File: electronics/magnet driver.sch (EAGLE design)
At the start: 16 parts, among them K1 G2RL-2DC12, Q1 RK7002BMT116, Q2 DMN1019UVT-7DMN1019UVT-7, Q3 PMBT2222A,215PMBT2222A,215

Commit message: Added MCU
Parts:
- added C6: 0.1uF, Zach:CAPACITOR0805
- added C7, C8: 10pF, Zach:CAPACITOR0805
- added J1: 1-770968-0, Zach:1-770968-0
- added J2: DF1BZ-8DP-2.5DSA, Zach:DF1BZ-8DP-2.5DSA
- added U1: ATMEGA328PB32-TQFP, Zach:ATMEGA328PB32-TQFP
- added XTAL1: 8 MHz, Zach:XRCGB
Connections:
- new net !RESET: J2.!RESET, U1.PC6
- new net MISO: J2.MISO, U1.PB4
- new net MOSI: J2.MOSI, U1.PB3
- new net RX: J2.RX, U1.PD0
- new net SCL: J1.SCL, U1.PC5
- new net SCLK: J2.SCLK, U1.PB5
- new net SDA: J1.SDA, U1.PC4
- new net TX: J2.TX, U1.PD1
- new net XTAL1: C7.P$2, U1.PB6, XTAL1.P$1
- new net XTAL2: C8.P$2, U1.PB7, XTAL1.P$2
- net +3V3: now also C6.P$2, J1.+3V3, J2.+3V3, U1.AREF, U1.AVCC, U1.VCC
- net GND: now also C6.P$1, C7.P$1, C8.P$1, J1.GND, J2.GND, U1.GND

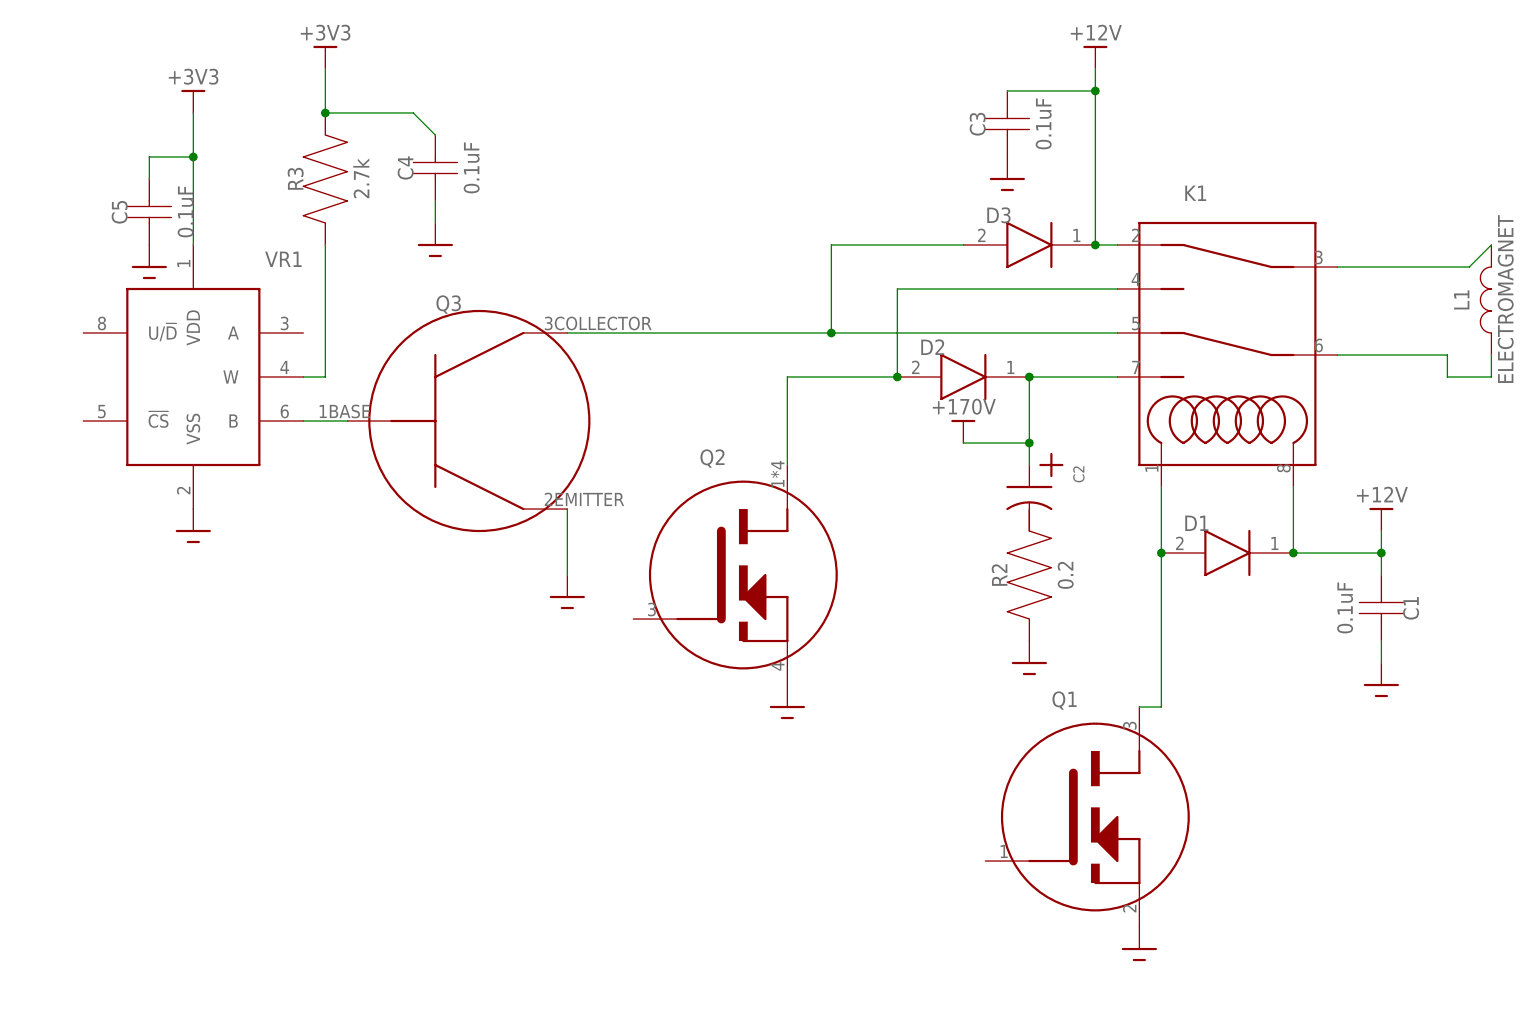
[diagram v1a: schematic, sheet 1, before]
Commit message: Finished magnet driver schematic
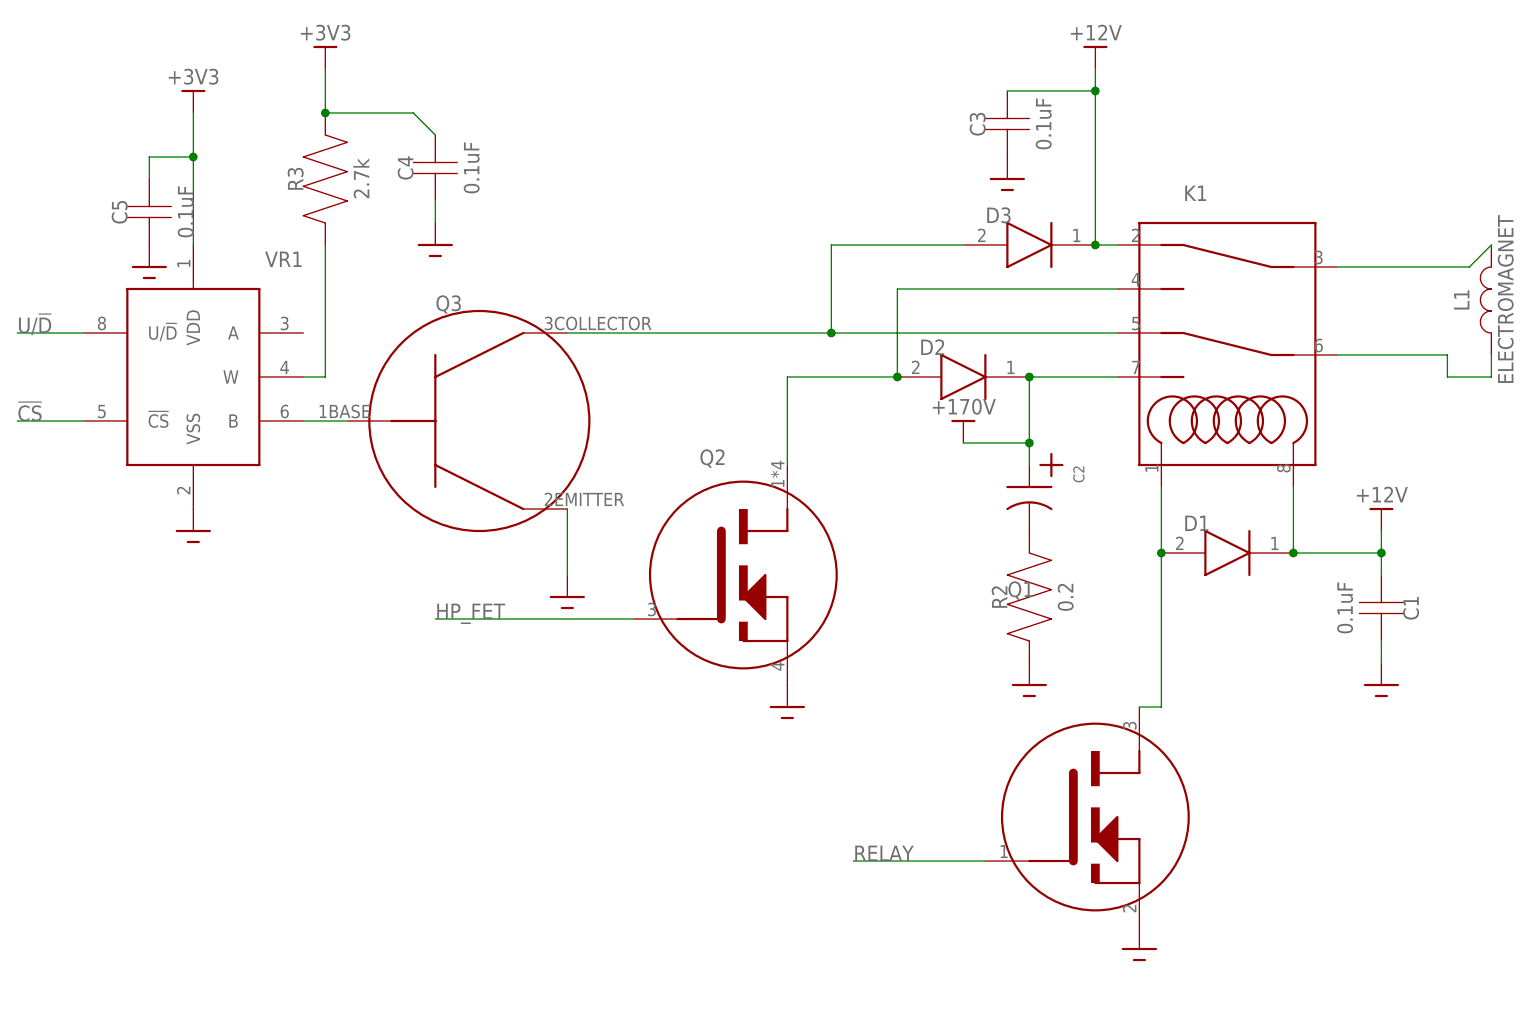
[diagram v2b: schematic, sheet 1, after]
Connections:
- new net !CS: U1.PD4, VR1.!CS
- new net HP_FET: Q2.GATE(1), U1.PD5
- new net N$2: C2.-, R2.P$2
- new net RELAY: Q1.GATE(1), U1.PD6
- new net U/!D: U1.PD3, VR1.U/!D
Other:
- moved on the sheet: R2
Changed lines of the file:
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@@
 <instance part="GND1" gate="1" x="119.38" y="-2.54" smashed="yes"/>
 <instance part="Q1" gate="G$1" x="99.06" y="-12.7" smashed="yes">
-<attribute name="NAME" x="81.28" y="-5.08" size="1.778" layer="95"/>
+<attribute name="NAME" x="76.2" y="7.62" size="1.778" layer="95"/>
 </instance>
 <instance part="GND2" gate="1" x="91.44" y="-33.02" smashed="yes"/>
@@
 <attribute name="NAME" x="66.04" y="35.56" size="1.778" layer="95"/>
 </instance>
-<instance part="GND3" gate="1" x="78.74" y="0" smashed="yes"/>
+<instance part="GND3" gate="1" x="78.74" y="-2.54" smashed="yes"/>
 <instance part="C2" gate="G$1" x="78.74" y="20.32" smashed="yes" rot="R270">
 <attribute name="NAME" x="83.82" y="22.86" size="1.27" layer="95" rot="R270"/>
 <attribute name="VALUE" x="73.66" y="22.86" size="1.27" layer="96" rot="R270"/>
 </instance>
-<instance part="R2" gate="G$1" x="78.74" y="2.54" smashed="yes" rot="R90">
-<attribute name="NAME" x="76.2" y="10.16" size="1.778" layer="95" rot="R90" align="bottom-center"/>
-<attribute name="VALUE" x="83.82" y="10.16" size="1.778" layer="96" rot="R90" align="bottom-center"/>
+<instance part="R2" gate="G$1" x="78.74" y="0" smashed="yes" rot="R90">
+<attribute name="NAME" x="76.2" y="7.62" size="1.778" layer="95" rot="R90" align="bottom-center"/>
+<attribute name="VALUE" x="83.82" y="7.62" size="1.778" layer="96" rot="R90" align="bottom-center"/>
 </instance>
 <instance part="P+2" gate="G$1" x="71.12" y="27.94" smashed="yes">
@@
 <junction x="-17.78" y="58.42"/>
 <pinref part="P+5" gate="G$1" pin="+3V3"/>
+</segment>
+</net>
+<net name="U/!D" class="0">
+<segment>
+<pinref part="VR1" gate="G$1" pin="U/!D"/>
+<wire x1="-30.48" y1="38.1" x2="-38.1" y2="38.1" width="0.1524" layer="91"/>
+<label x="-38.1" y="38.1" size="1.778" layer="95"/>
+</segment>
+</net>
+<net name="!CS" class="0">
+<segment>
+<pinref part="VR1" gate="G$1" pin="!CS"/>
+<wire x1="-30.48" y1="27.94" x2="-38.1" y2="27.94" width="0.1524" layer="91"/>
+<label x="-38.1" y="27.94" size="1.778" layer="95"/>
+</segment>
+</net>
+<net name="HP_FET" class="0">
+<segment>
+<pinref part="Q2" gate="G$1" pin="GATE(1)"/>
+<wire x1="33.02" y1="5.08" x2="10.16" y2="5.08" width="0.1524" layer="91"/>
+<label x="10.16" y="5.08" size="1.778" layer="95"/>
+</segment>
+</net>
+<net name="RELAY" class="0">
+<segment>
+<pinref part="Q1" gate="G$1" pin="GATE(1)"/>
+<wire x1="73.66" y1="-22.86" x2="58.42" y2="-22.86" width="0.1524" layer="91"/>
+<label x="58.42" y="-22.86" size="1.778" layer="95"/>
+</segment>
+</net>
+<net name="N$2" class="0">
+<segment>
+<pinref part="C2" gate="G$1" pin="-"/>
+<pinref part="R2" gate="G$1" pin="P$2"/>
 </segment>
 </net>
@@
 </segment>
 </net>
+<net name="U/!D" class="0">
+<segment>
+<pinref part="U1" gate="G$1" pin="PD3"/>
+<wire x1="68.58" y1="66.04" x2="81.28" y2="66.04" width="0.1524" layer="91"/>
+<label x="71.12" y="66.04" size="1.778" layer="95"/>
+</segment>
+</net>
+<net name="!CS" class="0">
+<segment>
+<pinref part="U1" gate="G$1" pin="PD4"/>
+<wire x1="68.58" y1="63.5" x2="81.28" y2="63.5" width="0.1524" layer="91"/>
+<label x="71.12" y="63.5" size="1.778" layer="95"/>
+</segment>
+</net>
+<net name="HP_FET" class="0">
+<segment>
+<pinref part="U1" gate="G$1" pin="PD5"/>
+<wire x1="68.58" y1="60.96" x2="81.28" y2="60.96" width="0.1524" layer="91"/>
+<label x="71.12" y="60.96" size="1.778" layer="95"/>
+</segment>
+</net>
+<net name="RELAY" class="0">
+<segment>
+<pinref part="U1" gate="G$1" pin="PD6"/>
+<wire x1="68.58" y1="58.42" x2="81.28" y2="58.42" width="0.1524" layer="91"/>
+<label x="71.12" y="58.42" size="1.778" layer="95"/>
+</segment>
+</net>

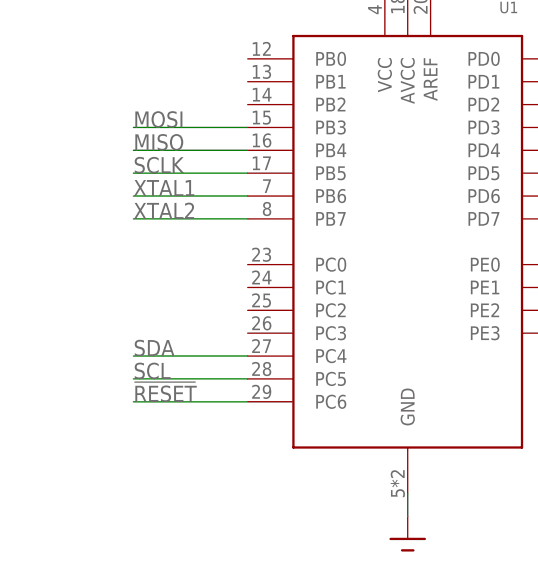
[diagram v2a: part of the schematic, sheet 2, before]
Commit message: Added pull-up on RESET
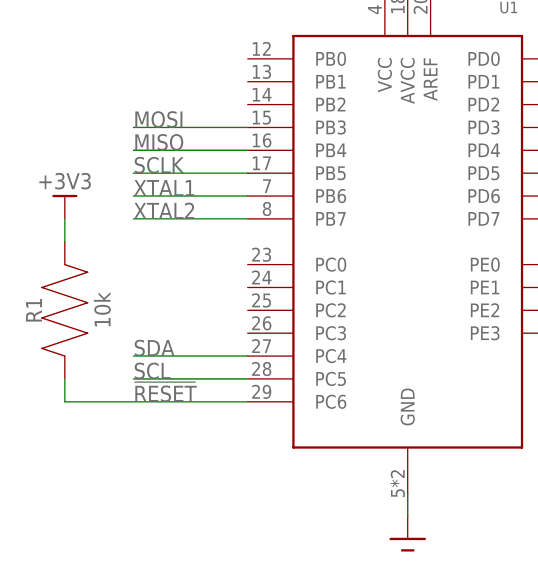
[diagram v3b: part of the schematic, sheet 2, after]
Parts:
- added R1: 10k, Zach:RESISTOR0805
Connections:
- net !RESET: now also R1.P$1
- net +3V3: now also R1.P$2
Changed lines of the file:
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@@
 <part name="GND14" library="Zach" deviceset="GND" device=""/>
 <part name="GND15" library="Zach" deviceset="GND" device=""/>
+<part name="R1" library="Zach" deviceset="RESISTOR" device="0805" value="10k"/>
+<part name="P+10" library="Zach" deviceset="+3V3" device=""/>
 </parts>
 <sheets>
@@
 <instance part="GND14" gate="1" x="86.36" y="22.86" smashed="yes"/>
 <instance part="GND15" gate="1" x="104.14" y="22.86" smashed="yes"/>
+<instance part="R1" gate="G$1" x="12.7" y="38.1" smashed="yes" rot="R90">
+<attribute name="NAME" x="10.16" y="45.72" size="1.778" layer="95" rot="R90" align="bottom-center"/>
+<attribute name="VALUE" x="17.78" y="45.72" size="1.778" layer="96" rot="R90" align="bottom-center"/>
+</instance>
+<instance part="P+10" gate="G$1" x="12.7" y="58.42" smashed="yes">
+<attribute name="VALUE" x="12.7" y="60.96" size="1.778" layer="96" rot="R180" align="bottom-center"/>
+</instance>
 </instances>
 <busses>
@@
 <wire x1="119.38" y1="55.88" x2="121.92" y2="55.88" width="0.1524" layer="91"/>
 </segment>
+<segment>
+<pinref part="R1" gate="G$1" pin="P$2"/>
+<pinref part="P+10" gate="G$1" pin="+3V3"/>
+<wire x1="12.7" y1="55.88" x2="12.7" y2="53.34" width="0.1524" layer="91"/>
+</segment>
 </net>
 <net name="GND" class="0">
@@
 <segment>
 <pinref part="U1" gate="G$1" pin="PC6"/>
-<wire x1="33.02" y1="35.56" x2="20.32" y2="35.56" width="0.1524" layer="91"/>
+<wire x1="33.02" y1="35.56" x2="12.7" y2="35.56" width="0.1524" layer="91"/>
 <label x="20.32" y="35.56" size="1.778" layer="95"/>
-</segment>
-</net>
+<pinref part="R1" gate="G$1" pin="P$1"/>
+<wire x1="12.7" y1="35.56" x2="12.7" y2="38.1" width="0.1524" layer="91"/>
+</segment>
+</net>

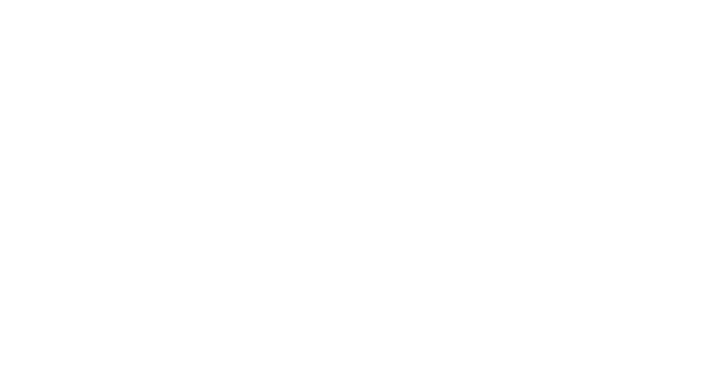
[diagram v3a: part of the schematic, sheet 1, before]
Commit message: Update magnet driver.sch
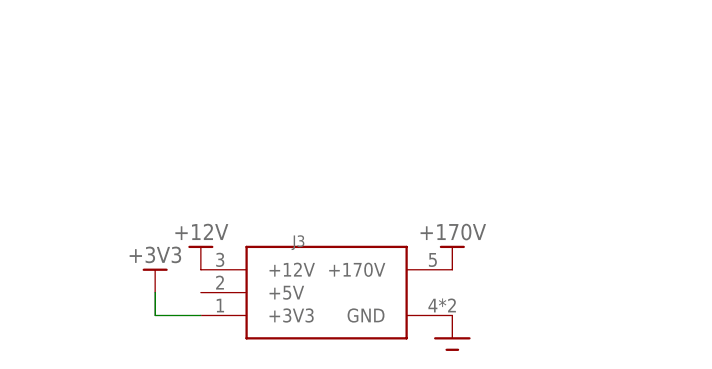
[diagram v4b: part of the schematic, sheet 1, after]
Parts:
- added J3: 1-770969-0, Zach:1-770969-0
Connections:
- net +12V: now also J3.+12V
- net +170V: now also J3.+170V
- net +3V3: now also J3.+3V3
- net GND: now also J3.GND
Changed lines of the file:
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@@
 <part name="R1" library="Zach" deviceset="RESISTOR" device="0805" value="10k"/>
 <part name="P+10" library="Zach" deviceset="+3V3" device=""/>
+<part name="J3" library="Zach" deviceset="1-770969-0" device=""/>
+<part name="GND16" library="Zach" deviceset="GND" device=""/>
+<part name="P+11" library="Zach" deviceset="+170V" device=""/>
+<part name="P+12" library="Zach" deviceset="+12V" device=""/>
+<part name="P+13" library="Zach" deviceset="+3V3" device=""/>
 </parts>
 <sheets>
@@
 </instance>
 <instance part="GND9" gate="1" x="-17.78" y="15.24" smashed="yes"/>
+<instance part="J3" gate="G$1" x="-17.78" y="-38.1" smashed="yes">
+<attribute name="NAME" x="-7.62" y="-27.94" size="1.27" layer="95"/>
+</instance>
+<instance part="GND16" gate="1" x="10.16" y="-38.1" smashed="yes"/>
+<instance part="P+11" gate="G$1" x="10.16" y="-27.94" smashed="yes">
+<attribute name="VALUE" x="10.16" y="-25.4" size="1.778" layer="96" rot="R180" align="bottom-center"/>
+</instance>
+<instance part="P+12" gate="G$1" x="-17.78" y="-27.94" smashed="yes">
+<attribute name="VALUE" x="-17.78" y="-25.4" size="1.778" layer="96" rot="R180" align="bottom-center"/>
+</instance>
+<instance part="P+13" gate="G$1" x="-22.86" y="-30.48" smashed="yes">
+<attribute name="VALUE" x="-22.86" y="-27.94" size="1.778" layer="96" rot="R180" align="bottom-center"/>
+</instance>
 </instances>
 <busses>
@@
 <pinref part="VR1" gate="G$1" pin="VSS"/>
 <pinref part="GND9" gate="1" pin="GND"/>
+</segment>
+<segment>
+<pinref part="J3" gate="G$1" pin="GND"/>
+<pinref part="GND16" gate="1" pin="GND"/>
 </segment>
 </net>
@@
 <pinref part="P+3" gate="G$1" pin="+12V"/>
 </segment>
+<segment>
+<pinref part="J3" gate="G$1" pin="+12V"/>
+<pinref part="P+12" gate="G$1" pin="+12V"/>
+</segment>
 </net>
 <net name="N$4" class="0">
@@
 <junction x="78.74" y="25.4"/>
 </segment>
+<segment>
+<pinref part="J3" gate="G$1" pin="+170V"/>
+<pinref part="P+11" gate="G$1" pin="+170V"/>
+</segment>
 </net>
 <net name="N$7" class="0">
@@
 <pinref part="P+5" gate="G$1" pin="+3V3"/>
 </segment>
-</net>
+<segment>
+<pinref part="J3" gate="G$1" pin="+3V3"/>
+<wire x1="-17.78" y1="-35.56" x2="-22.86" y2="-35.56" width="0.1524" layer="91"/>
+<pinref part="P+13" gate="G$1" pin="+3V3"/>
+<wire x1="-22.86" y1="-35.56" x2="-22.86" y2="-33.02" width="0.1524" layer="91"/>
+</segment>
+</net>
